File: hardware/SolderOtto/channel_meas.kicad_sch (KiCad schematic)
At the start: 57 parts, among them U901 OPA202, U902 LM358B, U903 74hc4053, U904 OPA202, U905 OPA202

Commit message: rework some shit
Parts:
- removed R903: 20k, Resistor_SMD:R_0603_1608Metric, symbol Device:R
- removed R907: 2k55, Resistor_SMD:R_0603_1608Metric, symbol Device:R
- added C915, C918: 100n, Capacitor_SMD:C_0603_1608Metric, symbol Device:C
- added C916: 47p, Capacitor_SMD:C_0603_1608Metric, symbol Device:C
- added C917: 1n, Capacitor_SMD:C_0603_1608Metric, symbol Device:C
- added C919, C920: 1u, Capacitor_SMD:C_0603_1608Metric, symbol Device:C
- added D904: BAT54SFILM, Package_TO_SOT_SMD:SOT-23, symbol mylib_diodes:BAT54SFILM
- added R932, R942: 590k, Resistor_SMD:R_0603_1608Metric, symbol Device:R
- added R933, R936, R939, R940, R941: 22k6, Resistor_SMD:R_0603_1608Metric, symbol Device:R
- added R935, R943: 2k7, Resistor_SMD:R_0603_1608Metric, symbol Device:R
- added R937: 2k2, Resistor_SMD:R_0603_1608Metric, symbol Device:R
- added TP904: T_{TIP}, TestPoint:TestPoint_Keystone_5015_Micro-Minature, symbol Connector:TestPoint
- added U906: OPA202, Package_SO:SOIC-8_3.9x4.9mm_P1.27mm, symbol mylib_ic:OPA206
- added U907: LM358B, Package_SO:SOIC-8_3.9x4.9mm_P1.27mm, symbol Amplifier_Operational:LM358
- added U908: 74hc4053, Package_SO:TSSOP-16_4.4x5mm_P0.65mm, symbol mylib_ic:74hc4053
- R902: value 20k -> 22k6; Digikey P20.0KHCT-ND -> P22.6KHCT-ND
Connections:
- net +3V3: now also C919.1, D904.2, U908.16 (VCC)
- net +8V: now also C915.1, U906.7 (V+)
- net -5V: now also C918.1, C920.1, U906.4 (V-), U908.7 (VEE)
- net COM: now also R940.1
- net GND: now also C915.2, C917.2, C918.2, C919.2, C920.2, D904.1, R942.2, R943.2, U908.6 (~{E}), U908.8 (GND)
- net IN-: no longer C902.1, R901.1, U901.2 (-), U903.14 (1Z)
- net LOAD1: now also R936.1; no longer R902.1
- net SEL3: now also U908.9 (S3); no longer U903.11 (1S)
- net TC: now also R902.1, R933.1, R939.1
- net at R918.2, R921.2: now also U907.7; no longer U902.1
- net at U903.1 (2Y1): now also R902.2
- net at U903.12 (1Y0): no longer R908.2
- net at U903.13 (1Y1): no longer R909.2
- net at U903.3 (3Y1): now also R909.2
- net at U903.5 (3Y0): now also R908.2; no longer R902.2
- net at R921.1, R924.2: now also U907.6 (-); no longer U902.2 (-)
- net at U902.3 (+): now also R935.2; no longer R917.2
- net T_{TIP} renamed T_{TIP}_{a}
- net select: no longer names the net of U903.4 (3Z)
- net select: now also C902.1, R901.1, U901.2 (-)
- new net: C916.2, R942.1, U906.3 (+), U908.15 (2Z)
- new net: R936.2, U908.2 (2Y0)
- new net: R940.2, U908.3 (3Y1)
- new net: R933.2, U908.1 (2Y1)
- new net: C916.1, R932.1, U906.2 (-), U908.4 (3Z)
- new net: R939.2, U908.5 (3Y0)
- new net: R937.1, R941.2, U902.1
- new net: R941.1, R943.1, U902.2 (-)
- new net: R932.2, R935.1, U906.6
- new net: R917.2, U907.5 (+)
- new net: U906.1 (NC), U906.5 (NC), U906.8 (NC)
- new net SEL4: U908.10 (2S)
- new net T_{TIP}_{b}: C917.1, D904.3, R937.2, TP904.1
- no-connect marks 0 -> 8
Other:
- moved on the sheet: C901, C902, C903, C904, C905, C906, C907, C908, C909, C910, D901, D902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

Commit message: save work
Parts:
- removed R940, R941: 22k6, Resistor_SMD:R_0603_1608Metric, symbol Device:R
- removed R942: 590k, Resistor_SMD:R_0603_1608Metric, symbol Device:R
- removed R943: 2k7, Resistor_SMD:R_0603_1608Metric, symbol Device:R
- added R903, R938: 590k, Resistor_SMD:R_0603_1608Metric, symbol Device:R
- added R907, R934: 22k6, Resistor_SMD:R_0603_1608Metric, symbol Device:R
- R932: value 590k -> 22k6; Digikey 311-590KHRCT-ND -> P22.6KHCT-ND
- R933, R939: value 22k6 -> 2k7; Digikey P22.6KHCT-ND -> P2.70KHCT-ND
- R935: value 2k7 -> 2k2; Digikey P2.70KHCT-ND -> A129692CT-ND
- R937: value 2k2 -> 22k6; Digikey A129692CT-ND -> P22.6KHCT-ND
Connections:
- net SEL3 is gone; now on net SEL1: U908.9 (S3)
- net SEL4 is gone; now on net SEL2: U908.10 (2S)
- net COM: now also R932.1
- net GND: now also R939.2, R938.2
- net LOAD1: now also R934.1; no longer R936.1
- net TC: now also R936.1, R907.1; no longer R933.1, R939.1
- net T_{TIP}_{b}: now also R935.2; no longer R937.2
- net at C916.2, U906.3 (+), U908.15 (2Z): now also R938.1
- net at R936.2: now also U908.1 (2Y1); no longer U908.2 (2Y0)
- net at U908.3 (3Y1): now also R932.2
- net at R933.2: now also U907.5 (+); no longer U908.1 (2Y1)
- net at R918.2, R921.2: now also U902.1; no longer U907.7
- net at C916.1, U906.2 (-), U908.4 (3Z): now also R903.1; no longer R932.1
- net at U908.5 (3Y0): now also R907.2; no longer R939.2
- net at R937.1: now also R939.1, U907.6 (-); no longer U902.1
- net at U902.2 (-): now also R921.1, R924.2
- net at U902.3 (+): now also R917.2; no longer R935.2
- new net: R934.2, U908.2 (2Y0)
- new net: R935.1, R937.2, U907.7
- new net: R903.2, R933.1, U906.6
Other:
- moved on the sheet: U902A

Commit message: rework pcb
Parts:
- added C921, C922: 100n, Capacitor_SMD:C_0603_1608Metric, symbol Device:C
- added unit 3 of U907
- added unit 1 of U907
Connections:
- net +8V: now also C922.1, U907.8 (V+)
- net -5V: now also C921.1, U907.4 (V-)
- net GND: now also C921.2, C922.2
- net at R918.2, R921.2: now also U907.7; no longer U902.1
- net at U907.5 (+): now also R917.2; no longer R933.2
- net at R937.1, R939.1: now also U902.2 (-); no longer U907.6 (-)
- net at R935.1, R937.2: now also U902.1; no longer U907.7
- net at R921.1, R924.2: now also U907.6 (-); no longer U902.2 (-)
- net at U902.3 (+): now also R933.2; no longer R917.2
- net SEL1 renamed SEL1_{a}
- net SEL1_{a}: no longer U908.9 (S3)
- net SEL2 renamed SEL2_{a}
- net SEL2_{a}: no longer U908.10 (2S)
- new net SEL1_{b}: U908.9 (S3)
- new net SEL2_{b}: U908.10 (2S)
- no-connect marks 8 -> 11
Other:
- moved on the sheet: U902A, U902C, U907B

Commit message: change some parts
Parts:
- U902: Digikey 296-LM358BIDGKRCT-ND -> 296-LM358BAIDRCT-ND
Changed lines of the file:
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@@
 			)
 		)
-		(property "Digikey" "296-LM358BIDGKRCT-ND"
+		(property "Digikey" "296-LM358BAIDRCT-ND"
 			(at 195.58 92.71 0)
 			(effects
@@
 			)
 		)
-		(property "Digikey" "296-LM358BIDGKRCT-ND"
+		(property "Digikey" "296-LM358BAIDRCT-ND"
 			(at 335.28 55.88 0)
 			(effects
@@
 			)
 		)
-		(property "Digikey" "296-LM358BIDGKRCT-ND"
+		(property "Digikey" "296-LM358BAIDRCT-ND"
 			(at 144.78 55.88 0)
 			(effects

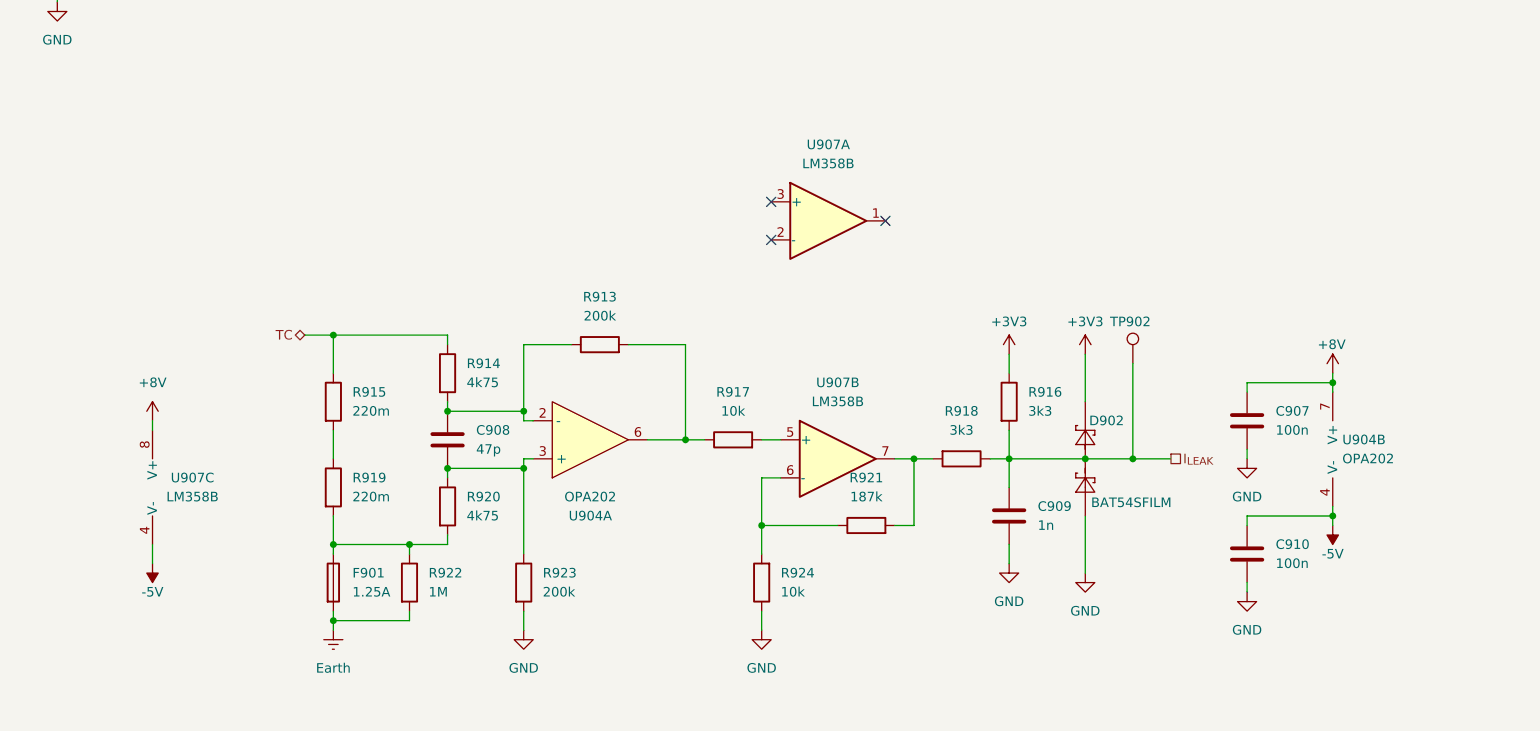
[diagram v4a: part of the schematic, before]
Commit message: remove 12V rail
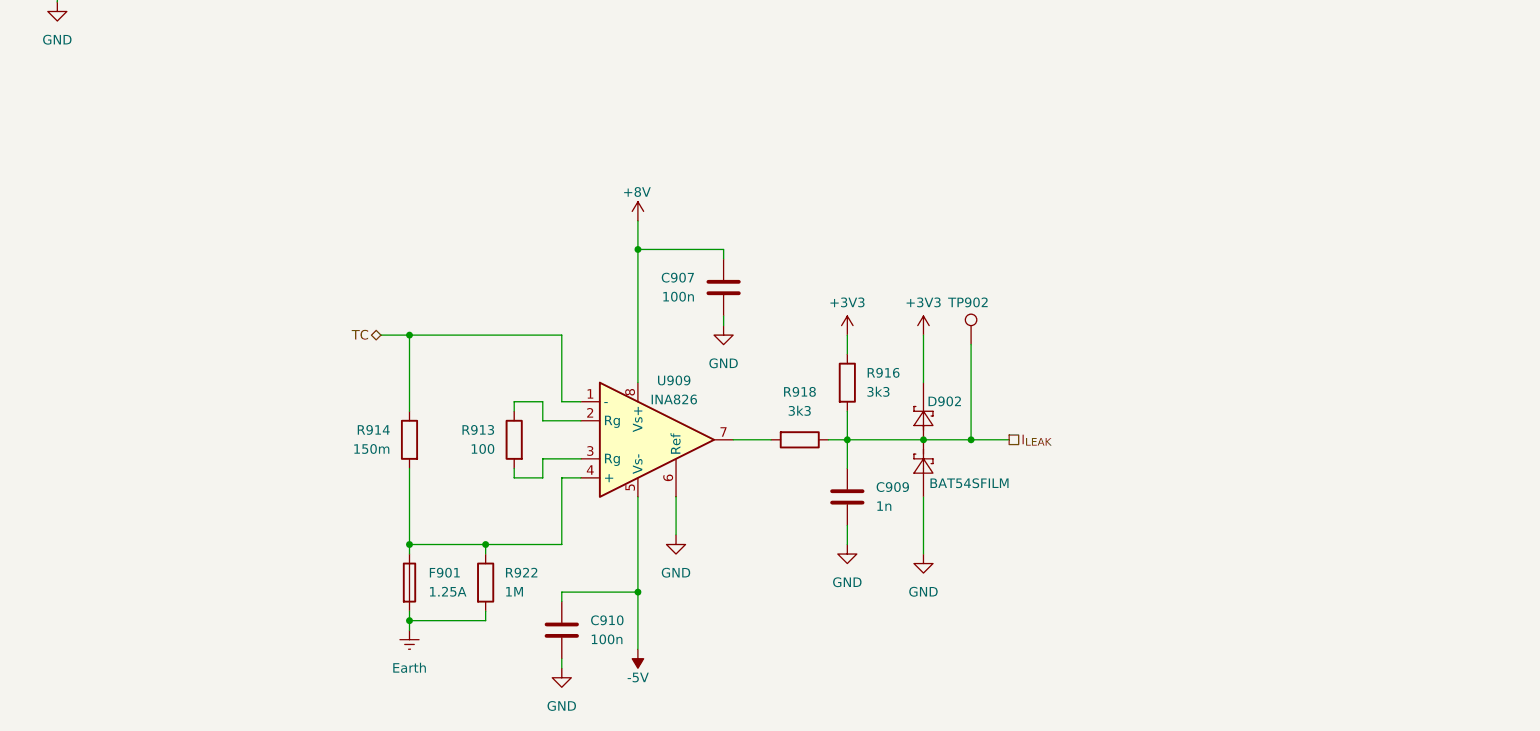
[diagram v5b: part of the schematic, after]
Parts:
- removed C908: 47p, Capacitor_SMD:C_0603_1608Metric, symbol Device:C
- removed R915, R919: 220m, Resistor_SMD:R_0805_2012Metric, symbol Device:R
- removed R917, R924: 10k, Resistor_SMD:R_0603_1608Metric, symbol Device:R
- removed R920: 4k75, Resistor_SMD:R_0603_1608Metric, symbol Device:R
- removed R921: 187k, Resistor_SMD:R_0603_1608Metric, symbol Device:R
- removed R923: 200k, Resistor_SMD:R_0603_1608Metric, symbol Device:R
- removed U904: OPA202, Package_SO:SOIC-8_3.9x4.9mm_P1.27mm, symbol mylib_ic:OPA206
- removed U907: LM358B, Package_SO:SOIC-8_3.9x4.9mm_P1.27mm, symbol Amplifier_Operational:LM358
- added U909: INA826, Package_SO:SOIC-8_3.9x4.9mm_P1.27mm, symbol mylib_ic:INA826
- R913: value 200k -> 100; footprint Resistor_SMD:R_0603_1608Metric -> Resistor_SMD:R_0805_2012Metric; Digikey 311-200KHRCT-ND -> (none)
- R914: value 4k75 -> 150m; footprint Resistor_SMD:R_0603_1608Metric -> Resistor_SMD:R_0805_2012Metric; Digikey P4.75KHCT-ND -> (none)
- R922: Digikey P1.00MHCT-ND -> 273-KDV12FR150ETCT-ND
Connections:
- net +8V: now also U909.8 (Vs+)
- net -5V: now also U909.5 (Vs-)
- net GND: now also U909.6 (Ref)
- net TC: now also U909.1 (-)
- net at R914.2: now also F901.1, R922.1, U909.4 (+); no longer R913.1
- net at R913.2: now also U909.3 (Rg)
- net at R918.2: now also U909.7
- new net: R913.1, U909.2 (Rg)
- no-connect marks 11 -> 8
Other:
- moved on the sheet: C907, C909, C910, D902, F901, R916, R918, R922, TP902

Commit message: save work
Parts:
- removed U903, U908: 74hc4053, Package_SO:TSSOP-16_4.4x5mm_P0.65mm, symbol mylib_ic:74hc4053
- added C907, C909, C912, C914: 100n, Capacitor_SMD:C_0603_1608Metric, symbol Device:C
- added JP901, JP902: SolderJumper_3_Open, Jumper:SolderJumper-3_P1.3mm_Open_RoundedPad1.0x1.5mm, symbol Jumper:SolderJumper_3_Open
- added U904, U905: TMUX4053, Package_SO:TSSOP-16_4.4x5mm_P0.65mm, symbol mylib_ic:TMUX4053
- renumbered C915 to C901, C916 to C903, C903 to C904, C917 to C905, C918 to C906, C905 to C908, C919 to C910, C906 to C911, C920 to C913, C901 to C915, C904 to C916, C922 to C917, C921 to C918, C907 to C919, C911 to C920, C912 to C921, C913 to C922, C909 to C923, C914 to C924, C910 to C925, D904 to D902, D902 to D904, R903 to R902, R908 to R903, R907 to R904, R909 to R905, R932 to R906, R904 to R907, R933 to R908, R905 to R909, R934 to R910, R906 to R911, R935 to R912, R902 to R913, R936 to R914, R910 to R915, R937 to R916, R911 to R917, R938 to R918, R912 to R919, R939 to R920, R925 to R921, R926 to R922, R916 to R923, R927 to R924, R928 to R925, R929 to R926, R914 to R927, R913 to R928, R918 to R929, R922 to R932, TP904 to TP902, TP902 to TP904, U906 to U902, U902 to U903, U905 to U906, U909 to U907
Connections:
- net +3V3: now also JP901.3 (B), JP902.3 (B); no longer C908.1, C910.1
- net -5V: now also C912.1, U904.7 (VEE), U905.7 (VEE)
- net GND: now also C907.2, C909.2, C912.2, U904.6 (~{E}), U904.8 (GND), U905.6 (~{E}), U905.8 (GND)
- net SEL1_{a}: now also U904.9 (S1)
- net SEL1_{b}: now also U905.9 (S1)
- net SEL2_{a}: now also U904.10 (S2)
- net SEL2_{b}: now also U905.10 (S2)
- net at R909.2: now also U904.2 (S2A)
- net at R914.2: now also U905.1 (S2B)
- net at C903.2, R918.1, U902.3 (+): now also U905.15 (D2)
- net at R910.2: now also U905.2 (S2A)
- net at R906.2: now also U905.3 (S1B)
- net at C903.1, R902.1, U902.2 (-): now also U905.4 (D1)
- net at R904.2: now also U905.5 (S1A)
- net at C902.2, R917.1, U901.3 (+): now also U904.15 (D2)
- net at R913.2: now also U904.1 (S2B)
- net at R905.2: now also U904.3 (S1B)
- net at C902.1, R901.1, U901.2 (-): now also U904.4 (D1)
- net at R903.2: now also U904.5 (S1A)
- new net: C907.1, C908.1, JP901.2 (C), U904.16 (VCC)
- new net: C909.1, C910.1, JP902.2 (C), U905.16 (VCC)
- new net +5V: JP901.1 (A), JP902.1 (A)
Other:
- moved on the sheet: C903, C905, C910, C915, C916, C917, C918, D902, R902, R904, R906, R908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

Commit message: rdy to route
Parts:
- removed JP901, JP902: SolderJumper_3_Open, Jumper:SolderJumper-3_P1.3mm_Open_RoundedPad1.0x1.5mm, symbol Jumper:SolderJumper_3_Open
- R927: footprint Resistor_SMD:R_0805_2012Metric -> Resistor_SMD:R_1206_3216Metric; Digikey (none) -> 283-MFHA1206R1500FCCT-ND
- R928: footprint Resistor_SMD:R_0805_2012Metric -> Resistor_SMD:R_0603_1608Metric
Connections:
- net +5V: now also C907.1, C908.1, C909.1, C910.1, U904.16 (VCC), U905.16 (VCC)
- net -5V: now also C914.1
- net GND: now also C914.2
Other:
- moved on the sheet: C914

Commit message: save wip
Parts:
- renumbered C901 to C801, C902 to C802, C903 to C803, C904 to C804, C905 to C805, C906 to C806, C907 to C807, C908 to C808, C909 to C809, C910 to C810, C911 to C811, C912 to C812, C913 to C813, C914 to C814, C915 to C815, C916 to C816, C917 to C817, C918 to C818, C919 to C819, C920 to C820, C921 to C821, C922 to C822, C923 to C823, C924 to C824, C925 to C825, D901 to D801, D902 to D802, D903 to D803, D904 to D804, F901 to F801, R901 to R801, R902 to R802, R903 to R803, R904 to R804, R905 to R805, R906 to R806, R907 to R807, R908 to R808, R909 to R809, R910 to R810, R911 to R811, R912 to R812, R913 to R813, R914 to R814, R915 to R815, R916 to R816, R917 to R817, R918 to R818, R919 to R819, R920 to R820, R921 to R821, R922 to R822, R923 to R823, R924 to R824, R925 to R825, R926 to R826, R927 to R827, R928 to R828, R929 to R829, R930 to R830, R931 to R831, R932 to R832, TP901 to TP801, TP902 to TP802, TP903 to TP803, TP904 to TP804, U901 to U801, U902 to U802, U903 to U803, U904 to U804, U905 to U805, U906 to U806, U907 to U807
